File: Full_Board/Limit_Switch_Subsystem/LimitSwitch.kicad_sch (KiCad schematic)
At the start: 7 parts, among them J7 OQ0212500000G, U7 UCLAMP3301H.TCT

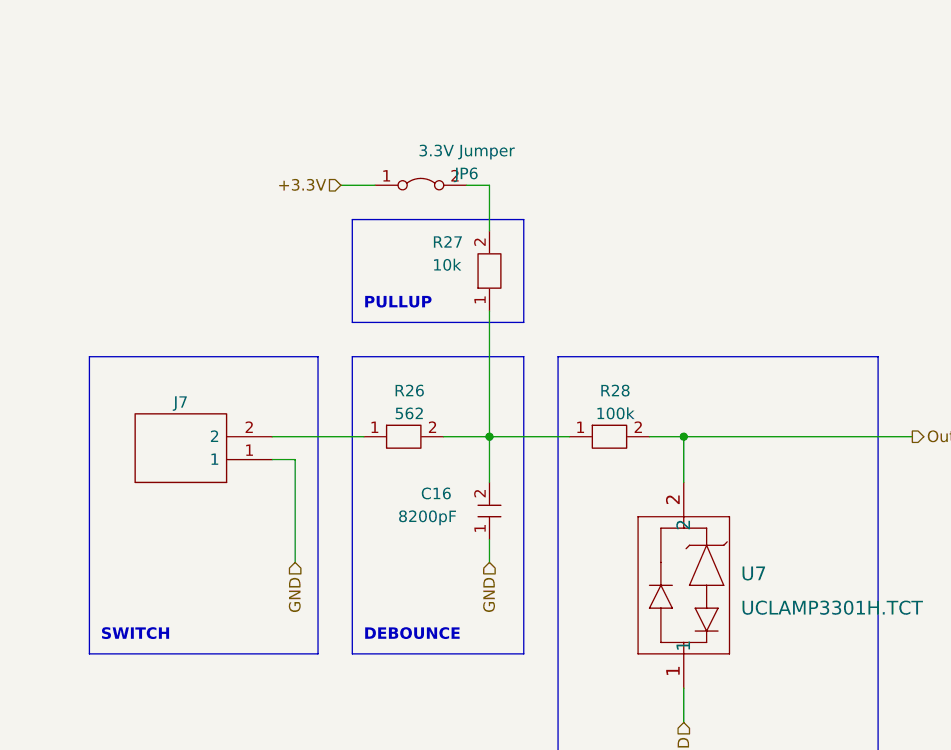
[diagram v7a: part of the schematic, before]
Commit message: Redo pinout, finish pcb layout (no traces)
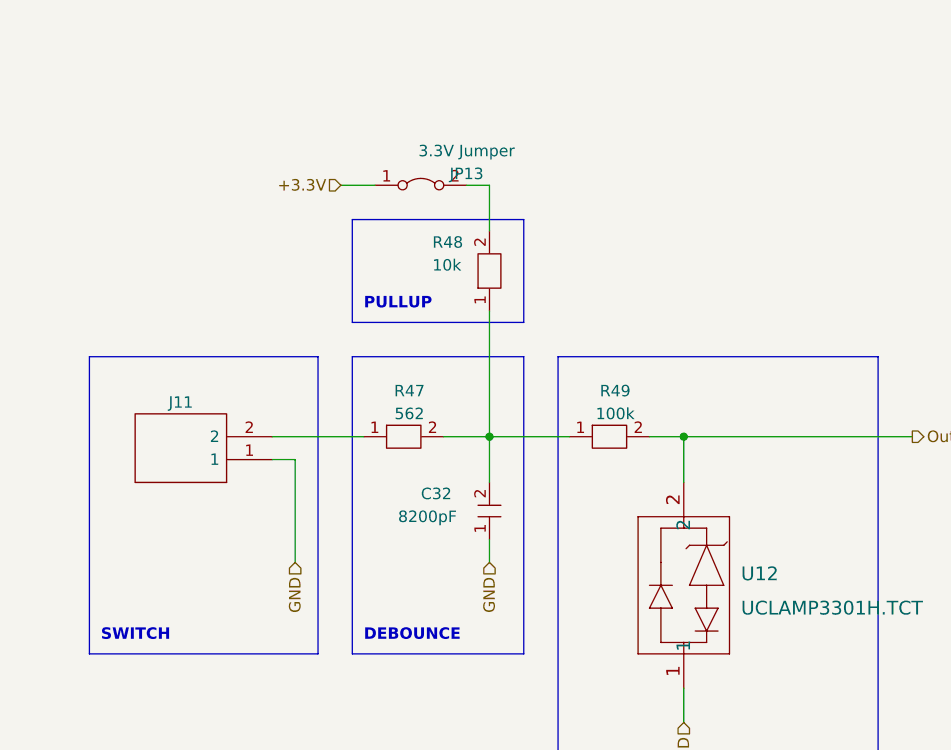
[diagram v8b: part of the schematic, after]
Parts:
- renumbered C16 to C32, J7 to J11, JP6 to JP13, R26 to R47, R27 to R48, R28 to R49, U7 to U12
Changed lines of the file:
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@@
     (effects (font (size 1.27 1.27)) (justify right))
   )
-  (symbol (lib_id "OQ0212500000G:OQ0212500000G") (at 119.38 92.71 180)
-    (in_bom yes) (on_board yes)
-    (property "Reference" "J7" (id 0) (at 109.22 86.36 0))
+  (symbol (lib_id "OQ0212500000G:OQ0212500000G") (at 119.38 92.71 180) (unit 1)
+    (in_bom yes) (on_board yes)
+    (property "Reference" "J11" (id 0) (at 109.22 86.36 0))
     (property "Value" "OQ0212500000G" (id 1) (at 109.22 85.09 0)
       (effects (font (size 1.27 1.27)) hide)
@@
     (pin "2")
   )
-  (symbol (lib_id "CR0402-FX-5620GLF:CR0402-FX-5620GLF") (at 129.54 90.17 0)
-    (in_bom yes) (on_board yes)
-    (property "Reference" "R26" (id 0) (at 134.62 85.09 0))
+  (symbol (lib_id "CR0402-FX-5620GLF:CR0402-FX-5620GLF") (at 129.54 90.17 0) (unit 1)
+    (in_bom yes) (on_board yes)
+    (property "Reference" "R47" (id 0) (at 134.62 85.09 0))
     (property "Value" "562" (id 1) (at 134.62 87.63 0))
     (property "Footprint" "CR0402-FX-5620GLF:RESC1005X40N" (id 2) (at 143.51 88.9 0)
@@
     (pin "2")
   )
-  (symbol (lib_id "RMCF1206FT10K0:10k") (at 143.51 76.2 90)
-    (in_bom yes) (on_board yes)
-    (property "Reference" "R27" (id 0) (at 137.16 68.58 90)
+  (symbol (lib_id "RMCF1206FT10K0:10k") (at 143.51 76.2 90) (unit 1)
+    (in_bom yes) (on_board yes)
+    (property "Reference" "R48" (id 0) (at 137.16 68.58 90)
       (effects (font (size 1.27 1.27)) (justify right))
     )
@@
     (pin "2")
   )
-  (symbol (lib_id "RCV2512100KFKEGAT:RCV2512100KFKEGAT") (at 152.4 90.17 0)
-    (in_bom yes) (on_board yes)
-    (property "Reference" "R28" (id 0) (at 157.48 85.09 0))
+  (symbol (lib_id "RCV2512100KFKEGAT:RCV2512100KFKEGAT") (at 152.4 90.17 0) (unit 1)
+    (in_bom yes) (on_board yes)
+    (property "Reference" "R49" (id 0) (at 157.48 85.09 0))
     (property "Value" "100k" (id 1) (at 157.48 87.63 0))
     (property "Footprint" "RCV2512100KFKEGAT:RESC6332X70N" (id 2) (at 166.37 88.9 0)
@@
     (pin "2")
   )
-  (symbol (lib_id "C1210C822K2RACAUTO:C1210C822K2RACAUTO") (at 143.51 101.6 90)
-    (in_bom yes) (on_board yes)
-    (property "Reference" "C16" (id 0) (at 135.89 96.52 90)
+  (symbol (lib_id "C1210C822K2RACAUTO:C1210C822K2RACAUTO") (at 143.51 101.6 90) (unit 1)
+    (in_bom yes) (on_board yes)
+    (property "Reference" "C32" (id 0) (at 135.89 96.52 90)
       (effects (font (size 1.27 1.27)) (justify right))
     )
@@
     (pin "2")
   )
-  (symbol (lib_id "Jumper:Jumper_2_Bridged") (at 135.89 62.23 0)
-    (in_bom yes) (on_board yes)
-    (property "Reference" "JP6" (id 0) (at 140.97 60.96 0))
+  (symbol (lib_id "Jumper:Jumper_2_Bridged") (at 135.89 62.23 0) (unit 1)
+    (in_bom yes) (on_board yes)
+    (property "Reference" "JP13" (id 0) (at 140.97 60.96 0))
     (property "Value" "3.3V Jumper" (id 1) (at 140.97 58.42 0))
     (property "Footprint" "TestPoint:TestPoint_2Pads_Pitch2.54mm_Drill0.8mm" (id 2) (at 135.89 62.23 0)
@@
     (pin "2")
   )
-  (symbol (lib_id "UCLAMP3301H-TCT:UCLAMP3301H.TCT") (at 165.1 127 90)
+  (symbol (lib_id "UCLAMP3301H-TCT:UCLAMP3301H.TCT") (at 165.1 127 90) (unit 1)
     (in_bom yes) (on_board yes) (fields_autoplaced)
-    (property "Reference" "U7" (id 0) (at 171.45 105.41 90)
+    (property "Reference" "U12" (id 0) (at 171.45 105.41 90)
       (effects (font (size 1.524 1.524)) (justify right))
     )
